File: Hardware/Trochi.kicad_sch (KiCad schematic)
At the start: 49 parts, among them IC1 ICM-42688-P, J1 JST PH, J2 JST-SH, J3 JST-SH, J4 JST-SH, J5 JST-SH, J6 JST_SH, Q1 AO3400A, Q2 AO3400A, Q3 AO3400A, Q4 AO3400A, Q5 AO3400A, SW1 SW_SPDT, U1 ME6211C33M5, U2 YX-SMD5020

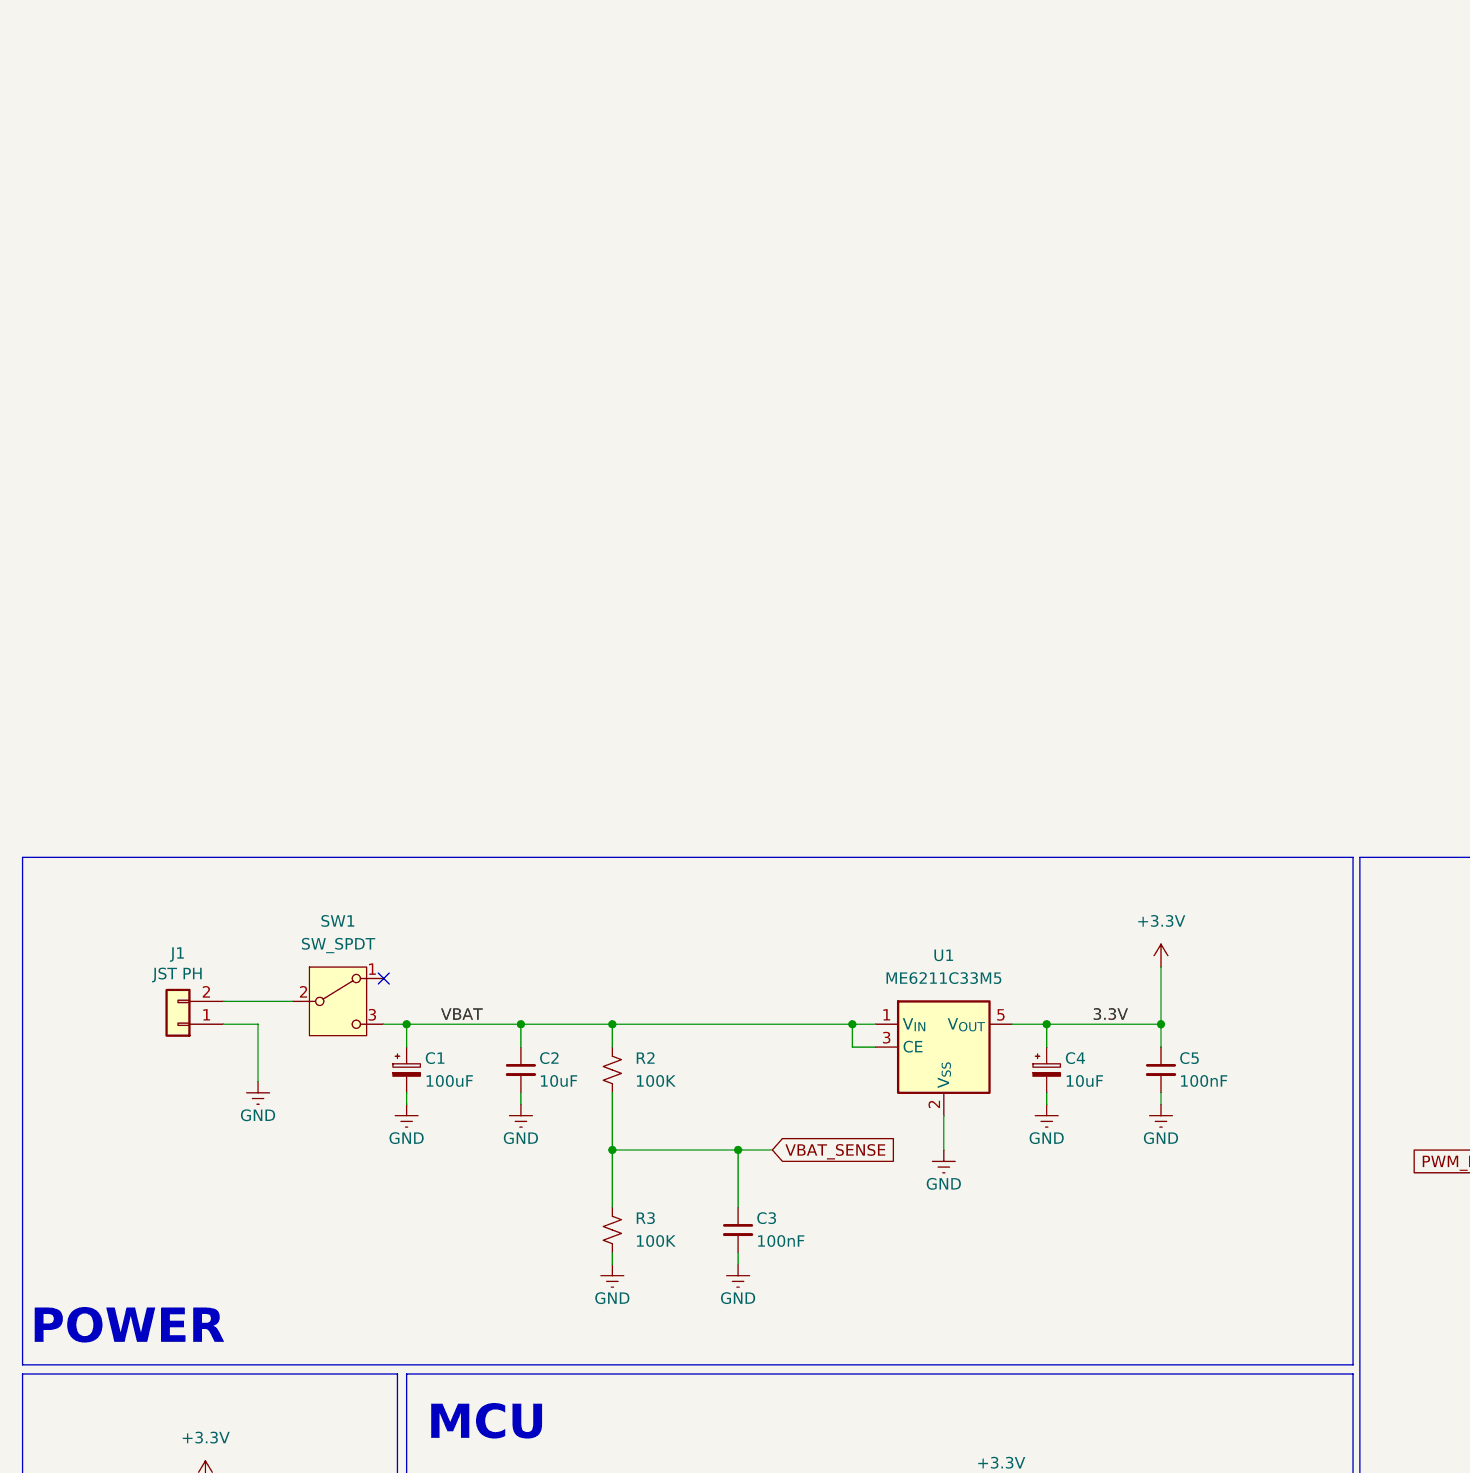
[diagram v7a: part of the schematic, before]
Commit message: feat: drive power switch with MOSFET in soft power circuit
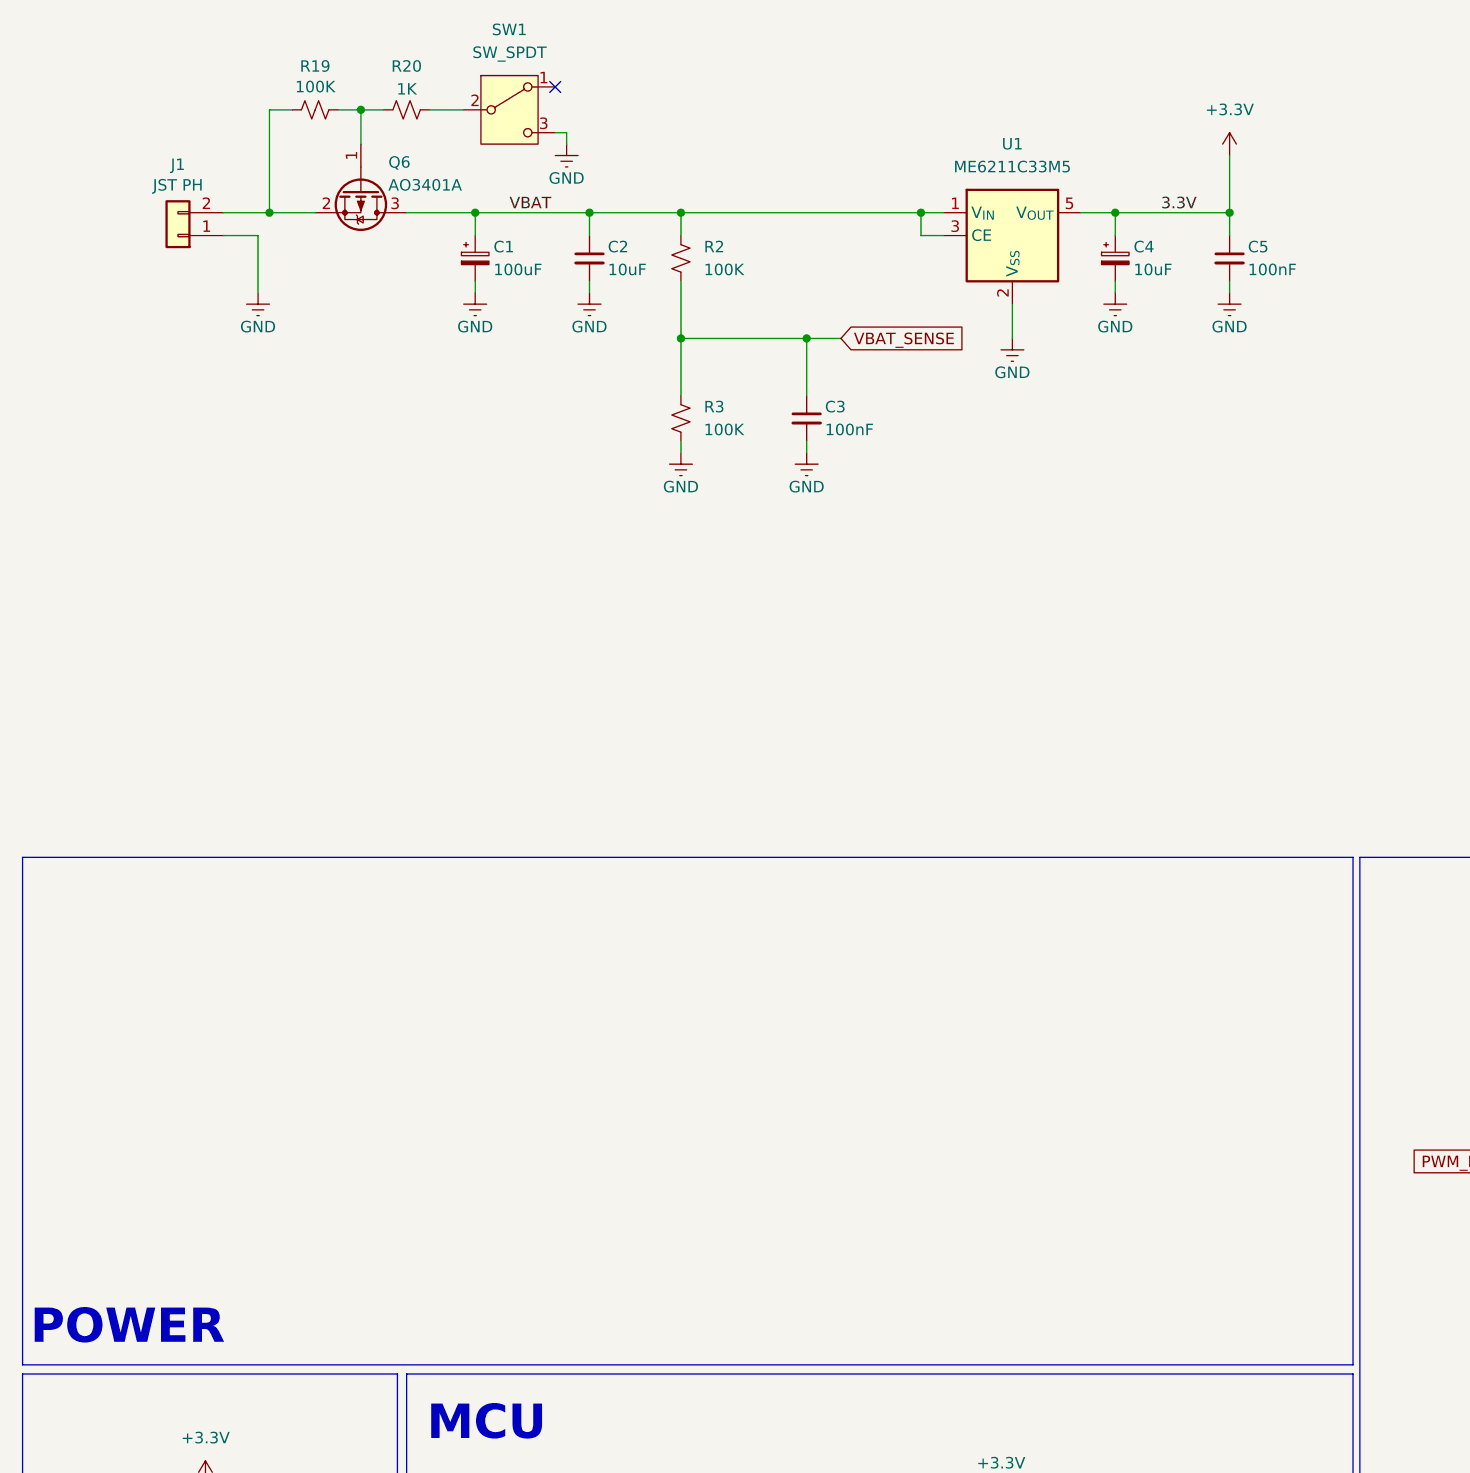
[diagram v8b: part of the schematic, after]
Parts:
- added Q6: AO3401A, Package_TO_SOT_SMD:SOT-23, symbol Transistor_FET:AO3401A
- added R19: 100K, symbol Device:R_Small_US
- added R20: 1K, symbol Device:R_Small_US
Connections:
- net GND: now also SW1.3 (C)
- net VBAT: now also Q6.3 (D); no longer SW1.3 (C)
- net at J1.2 (Pin_2): now also Q6.2 (S), R19.1; no longer SW1.2 (B)
- new net: Q6.1 (G), R19.2, R20.1
- new net: R20.2, SW1.2 (B)
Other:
- moved on the sheet: C1, C2, C3, C4, C5, R2, R3, U1
